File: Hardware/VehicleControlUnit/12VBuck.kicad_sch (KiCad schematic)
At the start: 12 parts, among them U3 LMR51635XDDCR

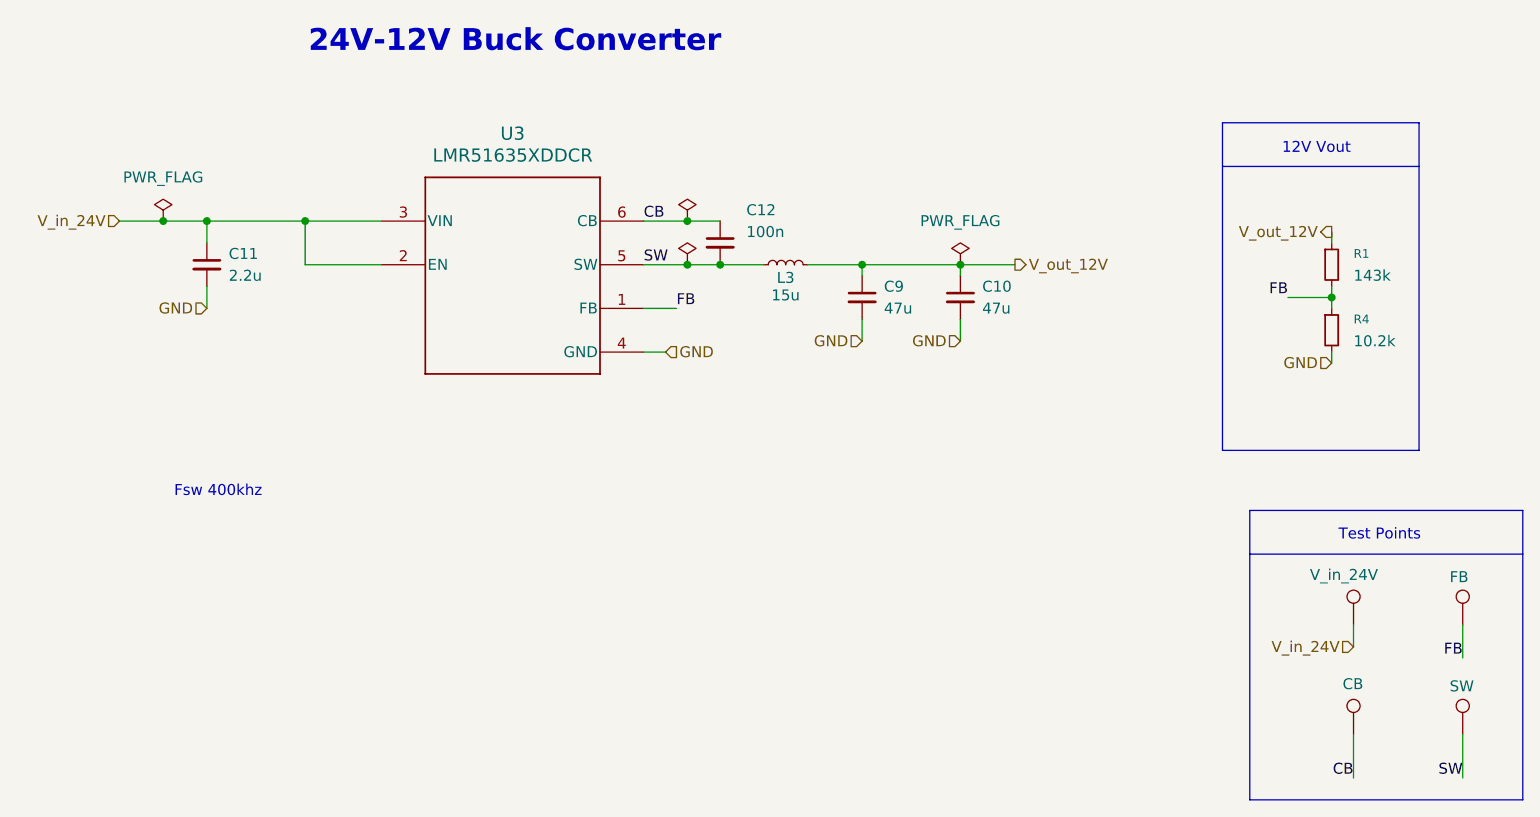
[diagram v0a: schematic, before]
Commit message: mcu pinouts todo - peripherals done
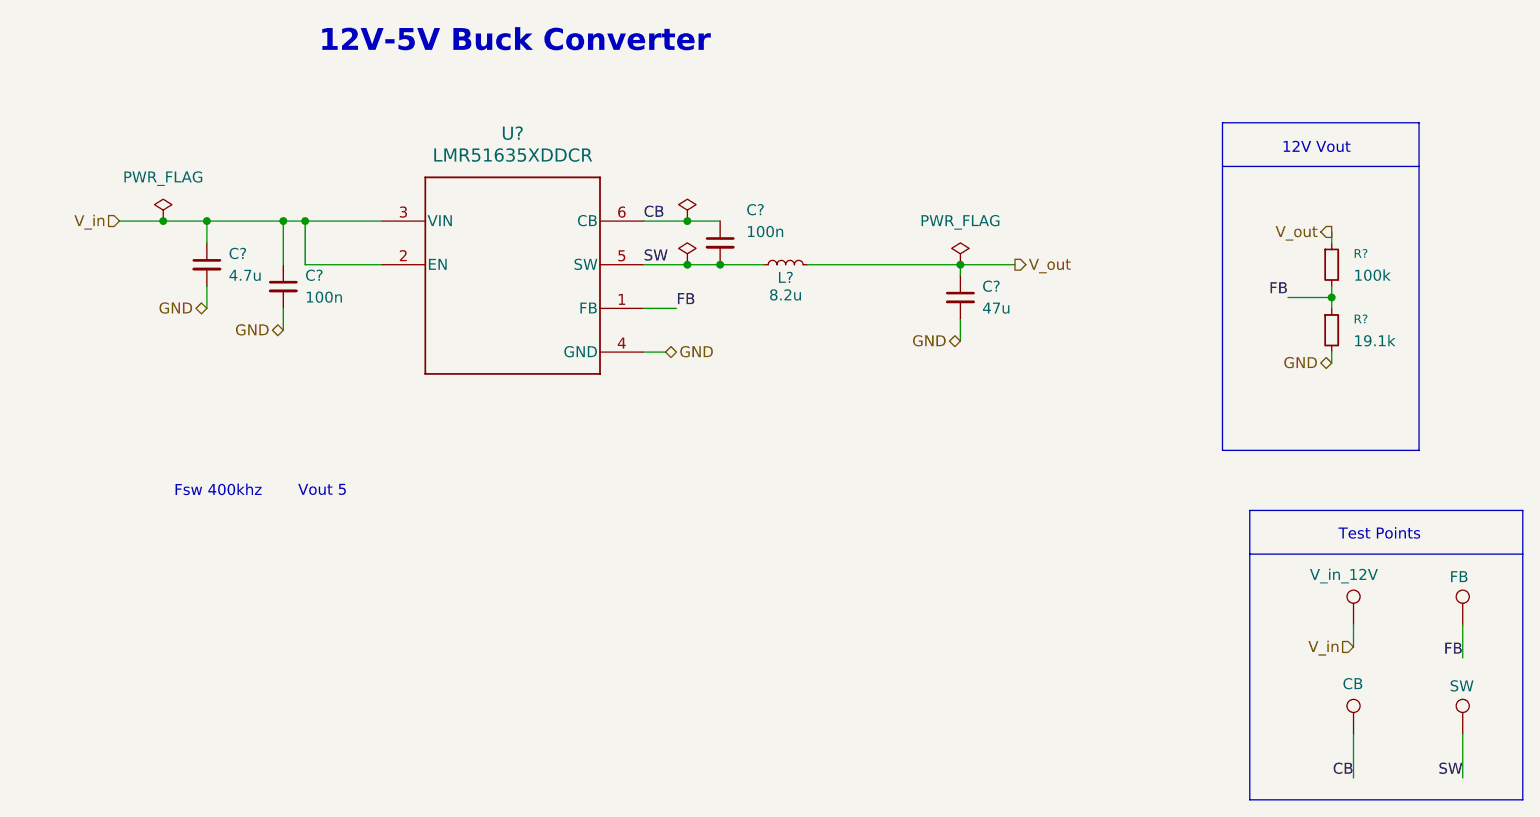
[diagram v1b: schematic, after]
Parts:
- removed C9: 47u, Capacitor_SMD:C_1210_3225Metric_Pad1.33x2.70mm_HandSolder, symbol Device:C_Small
- added C?: 100n, Capacitor_SMD:C_0805_2012Metric_Pad1.18x1.45mm_HandSolder, symbol Device:C_Small
- C?: renamed from C11; value 2.2u -> 4.7u; LCSC P/N C1771 -> (none); P/N CL21F225ZAFNNNE -> MSASL168SB5475KTNA01
- C?: renamed from C10; LCSC P/N C77101 -> (none); P/N GRM32ER61C476KE15L -> ZRB18AC80E476ME01L
- C?: renamed from C12; LCSC P/N C14663 -> (none)
- L?: renamed from L3; value 15u -> 8.2u; LCSC P/N C2849555 -> (none); P/N SRN8040-150M -> 74439369082
- R?: renamed from R1; value 143k -> 100k; LCSC P/N C22877 -> (none); P/N 0603WAF1433T5E -> AE1206BR-07100KL
- R?: renamed from R4; value 10.2k -> 19.1k; LCSC P/N C22772 -> (none); P/N 0603WAF1022T5E -> ERA-2ARB1912X
- TP?: renamed from TP9; value V_in_24V -> V_in_12V
- renumbered TP11 to TP?, TP10 to TP?, TP12 to TP?, U3 to U?
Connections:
- net GND: now also C?.2
- net V_in_24V renamed V_in
- net V_in: now also C?.1
- net V_out_12V renamed V_out
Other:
- note added: "12V-5V Buck Converter"
- note added: "Vout 5"
- note removed: "24V-12V Buck Converter"

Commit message: VCU more like diddle-u, mika time
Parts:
- gave numbers to parts that had none: 12
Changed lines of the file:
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@@
 		(dnp no)
 		(fields_autoplaced yes)
-		(property "Reference" "#FLG02"
+		(property "Reference" "#FLG07"
 			(at 149.86 79.375 0)
 			(hide yes)
@@
 			(project "VehicleControlUnit"
 				(path "/e864fac9-3897-46c9-9101-6d5488c6cd3a/f16a8bc3-f058-4d27-badd-0afc148d009e/dc3ab98d-8813-4545-9e4b-e0fd2f1fb432"
-					(reference "#FLG02")
+					(reference "#FLG07")
 					(unit 1)
 				)
@@
 		(dnp no)
 		(fields_autoplaced yes)
-		(property "Reference" "C?"
+		(property "Reference" "C1"
 			(at 96.52 85.0962 0)
 			(show_name no)
@@
 			(project "VehicleControlUnit"
 				(path "/e864fac9-3897-46c9-9101-6d5488c6cd3a/f16a8bc3-f058-4d27-badd-0afc148d009e/dc3ab98d-8813-4545-9e4b-e0fd2f1fb432"
-					(reference "C?")
+					(reference "C1")
 					(unit 1)
 				)
@@
 		(in_pos_files yes)
 		(dnp no)
-		(property "Reference" "TP?"
+		(property "Reference" "TP1"
 			(at 229.87 123.6979 0)
 			(hide yes)
@@
 			(project "VehicleControlUnit"
 				(path "/e864fac9-3897-46c9-9101-6d5488c6cd3a/f16a8bc3-f058-4d27-badd-0afc148d009e/dc3ab98d-8813-4545-9e4b-e0fd2f1fb432"
-					(reference "TP?")
+					(reference "TP1")
 					(unit 1)
 				)
@@
 		(in_pos_files yes)
 		(dnp no)
-		(property "Reference" "L?"
+		(property "Reference" "L1"
 			(at 161.29 87.884 90)
 			(show_name no)
@@
 			(project "VehicleControlUnit"
 				(path "/e864fac9-3897-46c9-9101-6d5488c6cd3a/f16a8bc3-f058-4d27-badd-0afc148d009e/dc3ab98d-8813-4545-9e4b-e0fd2f1fb432"
-					(reference "L?")
+					(reference "L1")
 					(unit 1)
 				)
@@
 		(in_pos_files yes)
 		(dnp no)
-		(property "Reference" "TP?"
+		(property "Reference" "TP3"
 			(at 242.57 123.6979 0)
 			(hide yes)
@@
 			(project "VehicleControlUnit"
 				(path "/e864fac9-3897-46c9-9101-6d5488c6cd3a/f16a8bc3-f058-4d27-badd-0afc148d009e/dc3ab98d-8813-4545-9e4b-e0fd2f1fb432"
-					(reference "TP?")
+					(reference "TP3")
 					(unit 1)
 				)
@@
 		(in_pos_files yes)
 		(dnp no)
-		(property "Reference" "TP?"
+		(property "Reference" "TP2"
 			(at 229.87 136.3979 0)
 			(hide yes)
@@
 			(project "VehicleControlUnit"
 				(path "/e864fac9-3897-46c9-9101-6d5488c6cd3a/f16a8bc3-f058-4d27-badd-0afc148d009e/dc3ab98d-8813-4545-9e4b-e0fd2f1fb432"
-					(reference "TP?")
+					(reference "TP2")
 					(unit 1)
 				)
@@
 		(dnp no)
 		(fields_autoplaced yes)
-		(property "Reference" "U?"
+		(property "Reference" "U1"
 			(at 129.54 71.12 0)
 			(show_name no)
@@
 			(project "VehicleControlUnit"
 				(path "/e864fac9-3897-46c9-9101-6d5488c6cd3a/f16a8bc3-f058-4d27-badd-0afc148d009e/dc3ab98d-8813-4545-9e4b-e0fd2f1fb432"
-					(reference "U?")
+					(reference "U1")
 					(unit 1)
 				)
@@
 		(in_pos_files yes)
 		(dnp no)
-		(property "Reference" "TP?"
+		(property "Reference" "TP4"
 			(at 242.57 136.3979 0)
 			(hide yes)
@@
 			(project "VehicleControlUnit"
 				(path "/e864fac9-3897-46c9-9101-6d5488c6cd3a/f16a8bc3-f058-4d27-badd-0afc148d009e/dc3ab98d-8813-4545-9e4b-e0fd2f1fb432"
-					(reference "TP?")
+					(reference "TP4")
 					(unit 1)
 				)
@@
 		(dnp no)
 		(fields_autoplaced yes)
-		(property "Reference" "C?"
+		(property "Reference" "C4"
 			(at 184.15 88.9062 0)
 			(show_name no)
@@
 			(project "VehicleControlUnit"
 				(path "/e864fac9-3897-46c9-9101-6d5488c6cd3a/f16a8bc3-f058-4d27-badd-0afc148d009e/dc3ab98d-8813-4545-9e4b-e0fd2f1fb432"
-					(reference "C?")
+					(reference "C4")
 					(unit 1)
 				)
@@
 		(dnp no)
 		(fields_autoplaced yes)
-		(property "Reference" "#FLG04"
+		(property "Reference" "#FLG09"
 			(at 181.61 84.455 0)
 			(hide yes)
@@
 			(project "VehicleControlUnit"
 				(path "/e864fac9-3897-46c9-9101-6d5488c6cd3a/f16a8bc3-f058-4d27-badd-0afc148d009e/dc3ab98d-8813-4545-9e4b-e0fd2f1fb432"
-					(reference "#FLG04")
+					(reference "#FLG09")
 					(unit 1)
 				)
@@
 		(dnp no)
 		(fields_autoplaced yes)
-		(property "Reference" "#FLG01"
+		(property "Reference" "#FLG06"
 			(at 88.9 79.375 0)
 			(hide yes)
@@
 			(project "VehicleControlUnit"
 				(path "/e864fac9-3897-46c9-9101-6d5488c6cd3a/f16a8bc3-f058-4d27-badd-0afc148d009e/dc3ab98d-8813-4545-9e4b-e0fd2f1fb432"
-					(reference "#FLG01")
+					(reference "#FLG06")
 					(unit 1)
 				)
@@
 		(in_pos_files yes)
 		(dnp no)
-		(property "Reference" "C?"
+		(property "Reference" "C3"
 			(at 156.718 80.01 0)
 			(show_name no)
@@
 			(project "VehicleControlUnit"
 				(path "/e864fac9-3897-46c9-9101-6d5488c6cd3a/f16a8bc3-f058-4d27-badd-0afc148d009e/dc3ab98d-8813-4545-9e4b-e0fd2f1fb432"
-					(reference "C?")
+					(reference "C3")
 					(unit 1)
 				)
@@
 		(in_pos_files yes)
 		(dnp no)
-		(property "Reference" "#FLG03"
+		(property "Reference" "#FLG08"
 			(at 149.86 84.455 0)
 			(hide yes)
@@
 			(project "VehicleControlUnit"
 				(path "/e864fac9-3897-46c9-9101-6d5488c6cd3a/f16a8bc3-f058-4d27-badd-0afc148d009e/dc3ab98d-8813-4545-9e4b-e0fd2f1fb432"
-					(reference "#FLG03")
+					(reference "#FLG08")
 					(unit 1)
 				)
@@
 		(dnp no)
 		(fields_autoplaced yes)
-		(property "Reference" "R?"
+		(property "Reference" "R1"
 			(at 227.33 85.0899 0)
 			(show_name no)
@@
 			(project "VehicleControlUnit"
 				(path "/e864fac9-3897-46c9-9101-6d5488c6cd3a/f16a8bc3-f058-4d27-badd-0afc148d009e/dc3ab98d-8813-4545-9e4b-e0fd2f1fb432"
-					(reference "R?")
+					(reference "R1")
 					(unit 1)
 				)
@@
 		(dnp no)
 		(fields_autoplaced yes)
-		(property "Reference" "C?"
+		(property "Reference" "C2"
 			(at 105.41 87.6362 0)
 			(show_name no)
@@
 			(project "VehicleControlUnit"
 				(path "/e864fac9-3897-46c9-9101-6d5488c6cd3a/f16a8bc3-f058-4d27-badd-0afc148d009e/dc3ab98d-8813-4545-9e4b-e0fd2f1fb432"
-					(reference "C?")
+					(reference "C2")
 					(unit 1)
 				)
@@
 		(dnp no)
 		(fields_autoplaced yes)
-		(property "Reference" "R?"
+		(property "Reference" "R2"
 			(at 227.33 92.7099 0)
 			(show_name no)
@@
 			(project "VehicleControlUnit"
 				(path "/e864fac9-3897-46c9-9101-6d5488c6cd3a/f16a8bc3-f058-4d27-badd-0afc148d009e/dc3ab98d-8813-4545-9e4b-e0fd2f1fb432"
-					(reference "R?")
-					(unit 1)
-				)
+					(reference "R2")
+					(unit 1)
+				)

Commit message: ughhhhhhhhhhhhhhhhhhh VCU will lokwey explode and propell the car
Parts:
- renumbered R1 to R5, R2 to R6
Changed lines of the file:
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@@
 		(dnp no)
 		(fields_autoplaced yes)
-		(property "Reference" "R1"
+		(property "Reference" "R5"
 			(at 227.33 85.0899 0)
 			(show_name no)
@@
 			(project "VehicleControlUnit"
 				(path "/e864fac9-3897-46c9-9101-6d5488c6cd3a/f16a8bc3-f058-4d27-badd-0afc148d009e/dc3ab98d-8813-4545-9e4b-e0fd2f1fb432"
-					(reference "R1")
+					(reference "R5")
 					(unit 1)
 				)
@@
 		(dnp no)
 		(fields_autoplaced yes)
-		(property "Reference" "R2"
+		(property "Reference" "R6"
 			(at 227.33 92.7099 0)
 			(show_name no)
@@
 			(project "VehicleControlUnit"
 				(path "/e864fac9-3897-46c9-9101-6d5488c6cd3a/f16a8bc3-f058-4d27-badd-0afc148d009e/dc3ab98d-8813-4545-9e4b-e0fd2f1fb432"
-					(reference "R2")
+					(reference "R6")
 					(unit 1)
 				)

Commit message: pre layout
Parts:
- removed C4: 47u, Capacitor_SMD:C_1210_3225Metric_Pad1.33x2.70mm_HandSolder, symbol Device:C_Small
- added C11, C12: 22u, Capacitor_SMD:C_1210_3225Metric_Pad1.33x2.70mm_HandSolder, symbol Device:C
- added C13: 3.3u, Capacitor_SMD:C_0805_2012Metric_Pad1.18x1.45mm_HandSolder, symbol Device:C
- C10: renamed from C3; LCSC P/N (none) -> C6666325
- C8: renamed from C1; LCSC P/N (none) -> C6962403; P/N MSASL168SB5475KTNA01 -> 08055D475KAT4A
- C9: renamed from C2; footprint Capacitor_SMD:C_0805_2012Metric_Pad1.18x1.45mm_HandSolder -> Capacitor_SMD:C_0603_1608Metric_Pad1.08x0.95mm_HandSolder; LCSC P/N (none) -> C6666325
- L1: footprint LHRS_Passives:SRN8040-150M -> LHRS_Passives:74439369082
- R11: renamed from R5; LCSC P/N (none) -> C25803; P/N AE1206BR-07100KL -> CRCW0603100KFKEE
- R12: renamed from R6; LCSC P/N (none) -> C844132; P/N ERA-2ARB1912X -> CRCW060319K1FKEAHP
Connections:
- net GND: now also C11.2, C12.2, C13.2
- net V_out: now also C11.1, C12.1, C13.1
